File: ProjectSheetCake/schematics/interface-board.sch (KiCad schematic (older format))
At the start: 44 parts, among them P1 CONN_8, P2 CONN_6, P3 CONN_8, P4 CONN_6, P7 X_Y_SERVO, P8 Z_A_SERVO

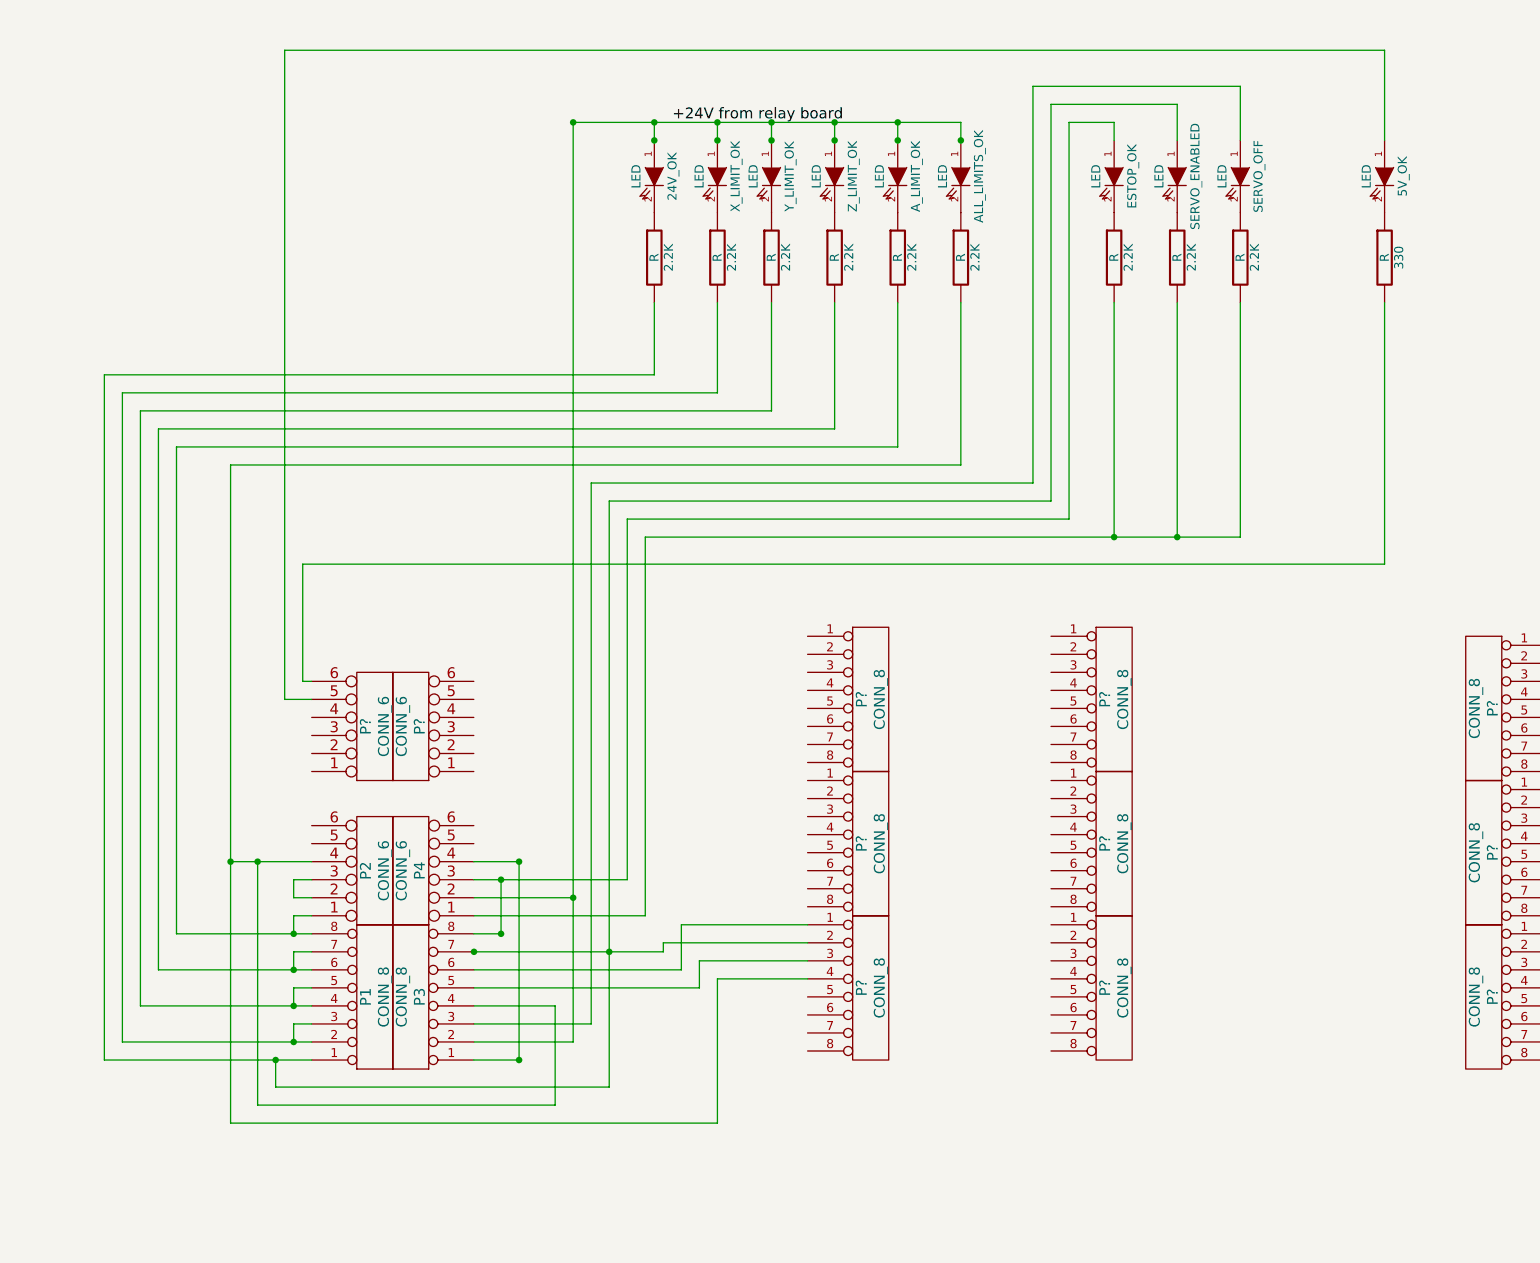
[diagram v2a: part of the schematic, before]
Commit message: Added on-board +5V to the mesa daughter boards
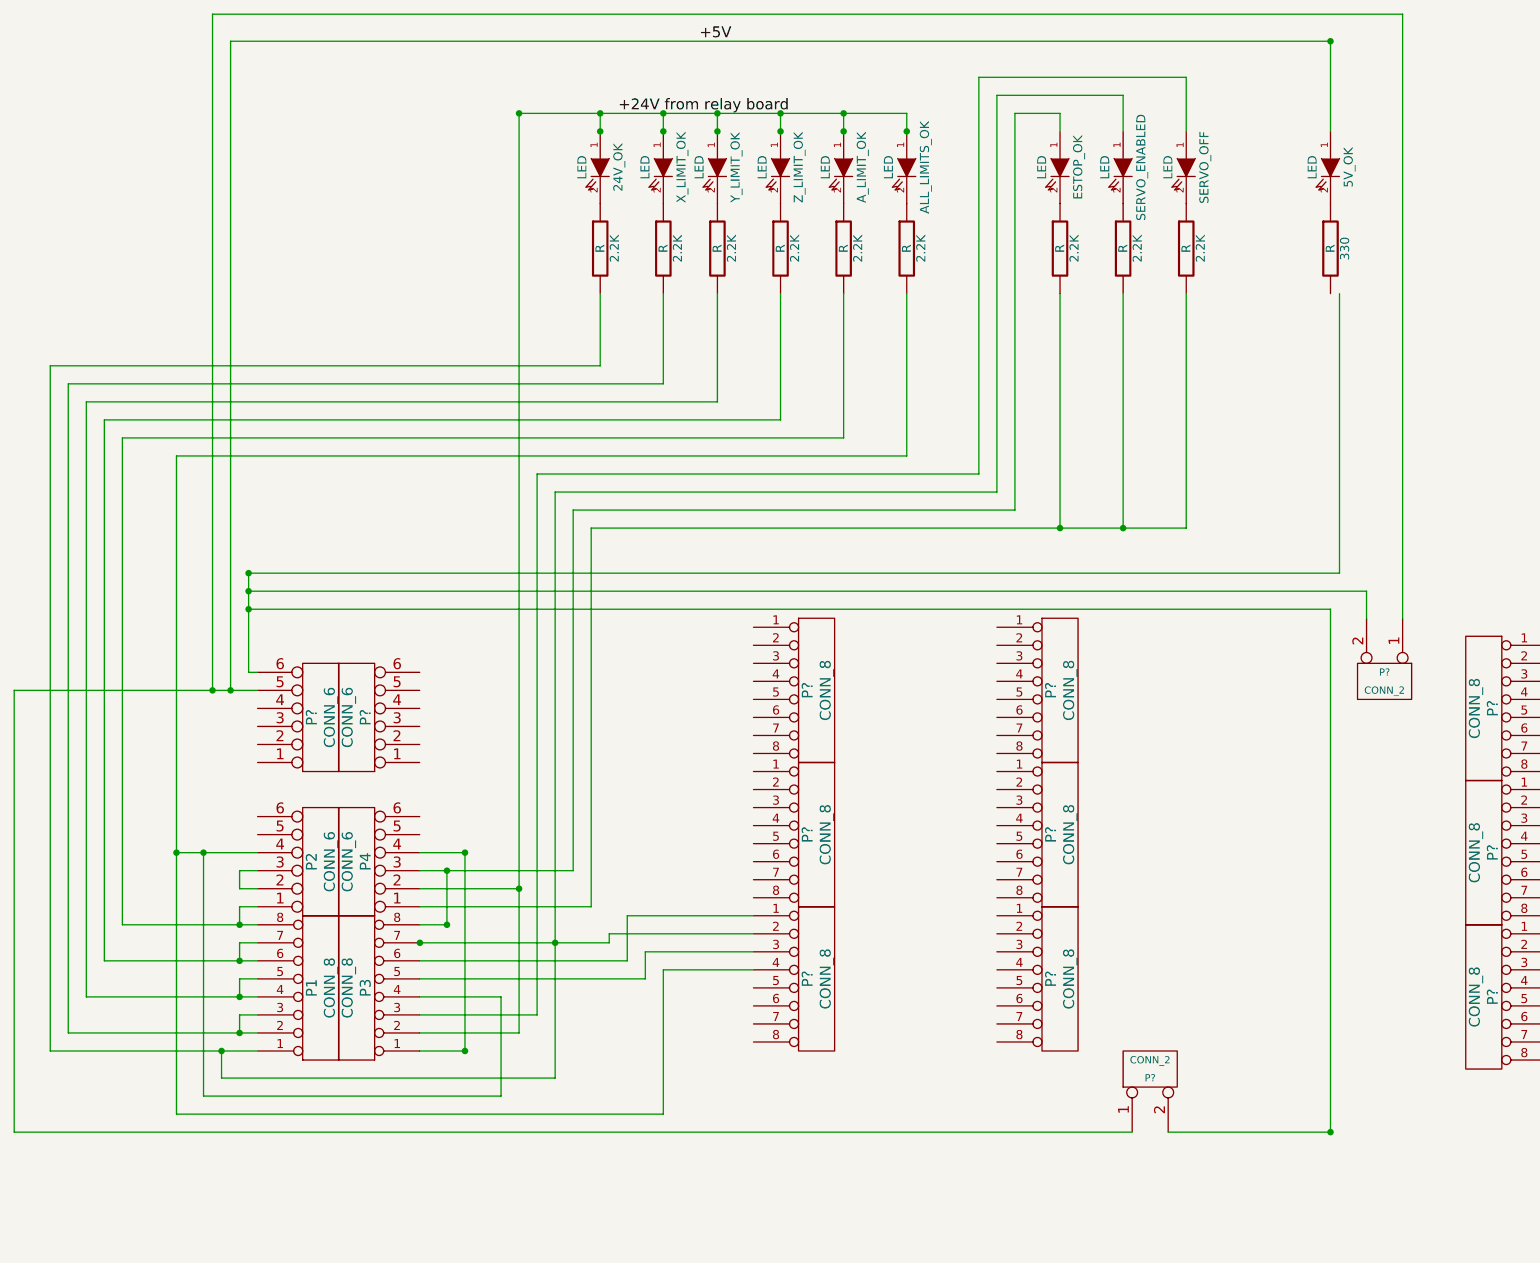
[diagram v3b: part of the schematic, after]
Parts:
- added P? (x2): CONN_2, symbol CONN_2
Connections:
- net labels added: +5V
- wire segments 252 -> 262
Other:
- moved on the sheet: 2.2K, 24V_OK, 330, 5V_OK, ALL_LIMITS_OK, A_LIMIT_OK, ESTOP_OK, P1, P2, P3, P4, P?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

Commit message: fixed an issue with the servo enable indicator LED
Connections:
- wire segments 262 -> 261

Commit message: fix up board layout
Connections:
- wire segments 261 -> 259
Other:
- moved on the sheet: P?
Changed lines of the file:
@@
-EESchema Schematic File Version 2  date 8/15/2011 12:07:04 AM
+EESchema Schematic File Version 2  date 8/15/2011 11:11:12 PM
 LIBS:power
 LIBS:device
@@
 Sheet 1 1
 Title ""
-Date "15 aug 2011"
+Date "16 aug 2011"
 Rev ""
 Comp ""
@@
 $EndDescr
 Wire Notes Line
-	4450 3600 4450 7050
+	11100 7050 8100 7050
 Wire Notes Line
-	7350 3600 4450 3600
+	11100 3600 8100 3600
+Wire Wire Line
+	8500 700  1700 700
+Wire Notes Line
+	4400 3600 7350 3600
+Wire Notes Line
+	4400 3600 4400 7050
+Wire Wire Line
+	4850 5950 4100 5950
+Connection ~ 4000 5750
+Wire Wire Line
+	4000 5750 4850 5750
+Wire Wire Line
+	2850 5850 4850 5850
 Wire Notes Line
 	7350 3600 7350 7050
-Wire Notes Line
-	7800 3600 7800 7050
-Wire Notes Line
-	7800 3600 11100 3600
 Wire Wire Line
 	6750 3350 4000 3350
@@
 	600  6900 6800 6900
 Wire Wire Line
-	8100 4050 8100 3900
+	8300 4050 8300 3900
 Wire Wire Line
 	1900 3800 1900 4350
@@
 Connection ~ 1900 3800
 Wire Wire Line
-	8100 3900 1900 3900
-Wire Wire Line
 	1900 4350 1950 4350
 Wire Wire Line
 	3600 6600 1750 6600
-Wire Wire Line
-	2850 5850 3900 5850
 Connection ~ 2850 5850
 Wire Wire Line
@@
 	11000 1950 12500 1950
 Wire Wire Line
-	12500 1950 12500 1550
-Wire Wire Line
 	10500 5000 10600 5000
 Wire Wire Line
@@
 	3850 1350 3850 1250
 Wire Wire Line
-	4000 5700 4700 5700
-Wire Wire Line
 	2850 5950 4000 5950
 Wire Wire Line
 	1750 6600 1750 6450
 Wire Wire Line
-	4100 5900 4100 6050
-Wire Wire Line
 	1950 5350 1500 5350
 Wire Wire Line
 	1500 6800 4200 6800
 Wire Wire Line
-	4200 6800 4200 6000
-Wire Wire Line
-	4200 6000 4700 6000
-Wire Wire Line
 	2849 6450 3099 6450
 Wire Wire Line
@@
 	3400 1250 5550 1250
 Wire Wire Line
-	4100 5900 4700 5900
-Wire Wire Line
-	4100 6050 2850 6050
+	2850 6050 4100 6050
 Wire Wire Line
 	2850 6150 3300 6150
@@
 	1650 6700 1650 5350
 Connection ~ 1650 5350
-Wire Wire Line
-	3900 5850 3900 5800
-Wire Wire Line
-	3900 5800 4700 5800
 Connection ~ 3000 5750
 Connection ~ 3000 5450
@@
 	7150 4000 7150 6900
 Wire Wire Line
-	8300 4050 8300 700
-Wire Wire Line
-	8300 700  1700 700
+	8500 700  8500 4050
 Wire Wire Line
 	1700 700  1700 4450
@@
 Wire Wire Line
 	4000 5950 4000 3350
-Connection ~ 4000 5700
-Wire Notes Line
-	7350 7050 4450 7050
 Wire Notes Line
 	11100 3600 11100 7050
+Wire Wire Line
+	12500 1950 12500 1500
+Wire Wire Line
+	4850 6050 4200 6050
+Wire Wire Line
+	4200 6050 4200 6800
+Wire Wire Line
+	4100 6050 4100 5950
 Wire Notes Line
-	11100 7050 7800 7050
+	7350 7050 4400 7050
+Wire Wire Line
+	8300 3900 1900 3900
+Wire Notes Line
+	8100 3600 8100 7050
 $Comp
 L CONN_2 P?
@@
 L CONN_2 P?
 U 1 1 4E4601E7
-P 8200 4400
-F 0 "P?" V 8150 4400 40  0000 C CNN
-F 1 "CONN_2" V 8250 4400 40  0000 C CNN
-	1    8200 4400
+P 8400 4400
+F 0 "P?" V 8350 4400 40  0000 C CNN
+F 1 "CONN_2" V 8450 4400 40  0000 C CNN
+	1    8400 4400
 	0    1    1    0
 $EndComp
@@
 L CONN_8 P?
 U 1 1 4E3F5325
-P 6400 6050
-F 0 "P?" V 6350 6050 60  0000 C CNN
-F 1 "CONN_8" V 6450 6050 60  0000 C CNN
-	1    6400 6050
+P 6550 6100
+F 0 "P?" V 6500 6100 60  0000 C CNN
+F 1 "CONN_8" V 6600 6100 60  0000 C CNN
+	1    6550 6100
 	1    0    0    -1
 $EndComp
@@
 L CONN_8 P?
 U 1 1 4E3F5321
-P 6400 5250
-F 0 "P?" V 6350 5250 60  0000 C CNN
-F 1 "CONN_8" V 6450 5250 60  0000 C CNN
-	1    6400 5250
+P 6550 5300
+F 0 "P?" V 6500 5300 60  0000 C CNN
+F 1 "CONN_8" V 6600 5300 60  0000 C CNN
+	1    6550 5300
 	1    0    0    -1
 $EndComp
@@
 L CONN_8 P?
 U 1 1 4E3F531C
-P 6400 4450
-F 0 "P?" V 6350 4450 60  0000 C CNN
-F 1 "CONN_8" V 6450 4450 60  0000 C CNN
-	1    6400 4450
+P 6550 4500
+F 0 "P?" V 6500 4500 60  0000 C CNN
+F 1 "CONN_8" V 6600 4500 60  0000 C CNN
+	1    6550 4500
 	1    0    0    -1
 $EndComp
@@
 L CONN_8 P?
 U 1 1 4E3F5317
-P 5050 6050
-F 0 "P?" V 5000 6050 60  0000 C CNN
-F 1 "CONN_8" V 5100 6050 60  0000 C CNN
-	1    5050 6050
+P 5200 6100
+F 0 "P?" V 5150 6100 60  0000 C CNN
+F 1 "CONN_8" V 5250 6100 60  0000 C CNN
+	1    5200 6100
 	1    0    0    -1
 $EndComp
@@
 L CONN_8 P?
 U 1 1 4E3F5313
-P 5050 5250
-F 0 "P?" V 5000 5250 60  0000 C CNN
-F 1 "CONN_8" V 5100 5250 60  0000 C CNN
-	1    5050 5250
+P 5200 5300
+F 0 "P?" V 5150 5300 60  0000 C CNN
+F 1 "CONN_8" V 5250 5300 60  0000 C CNN
+	1    5200 5300
 	1    0    0    -1
 $EndComp
@@
 L CONN_8 P?
 U 1 1 4E3F530D
-P 5050 4450
-F 0 "P?" V 5000 4450 60  0000 C CNN
-F 1 "CONN_8" V 5100 4450 60  0000 C CNN
-	1    5050 4450
-	1    0    0    -1
-$EndComp
+P 5200 4500
+F 0 "P?" V 5150 4500 60  0000 C CNN
+F 1 "CONN_8" V 5250 4500 60  0000 C CNN
+	1    5200 4500
+	1    0    0    -1
+$EndComp

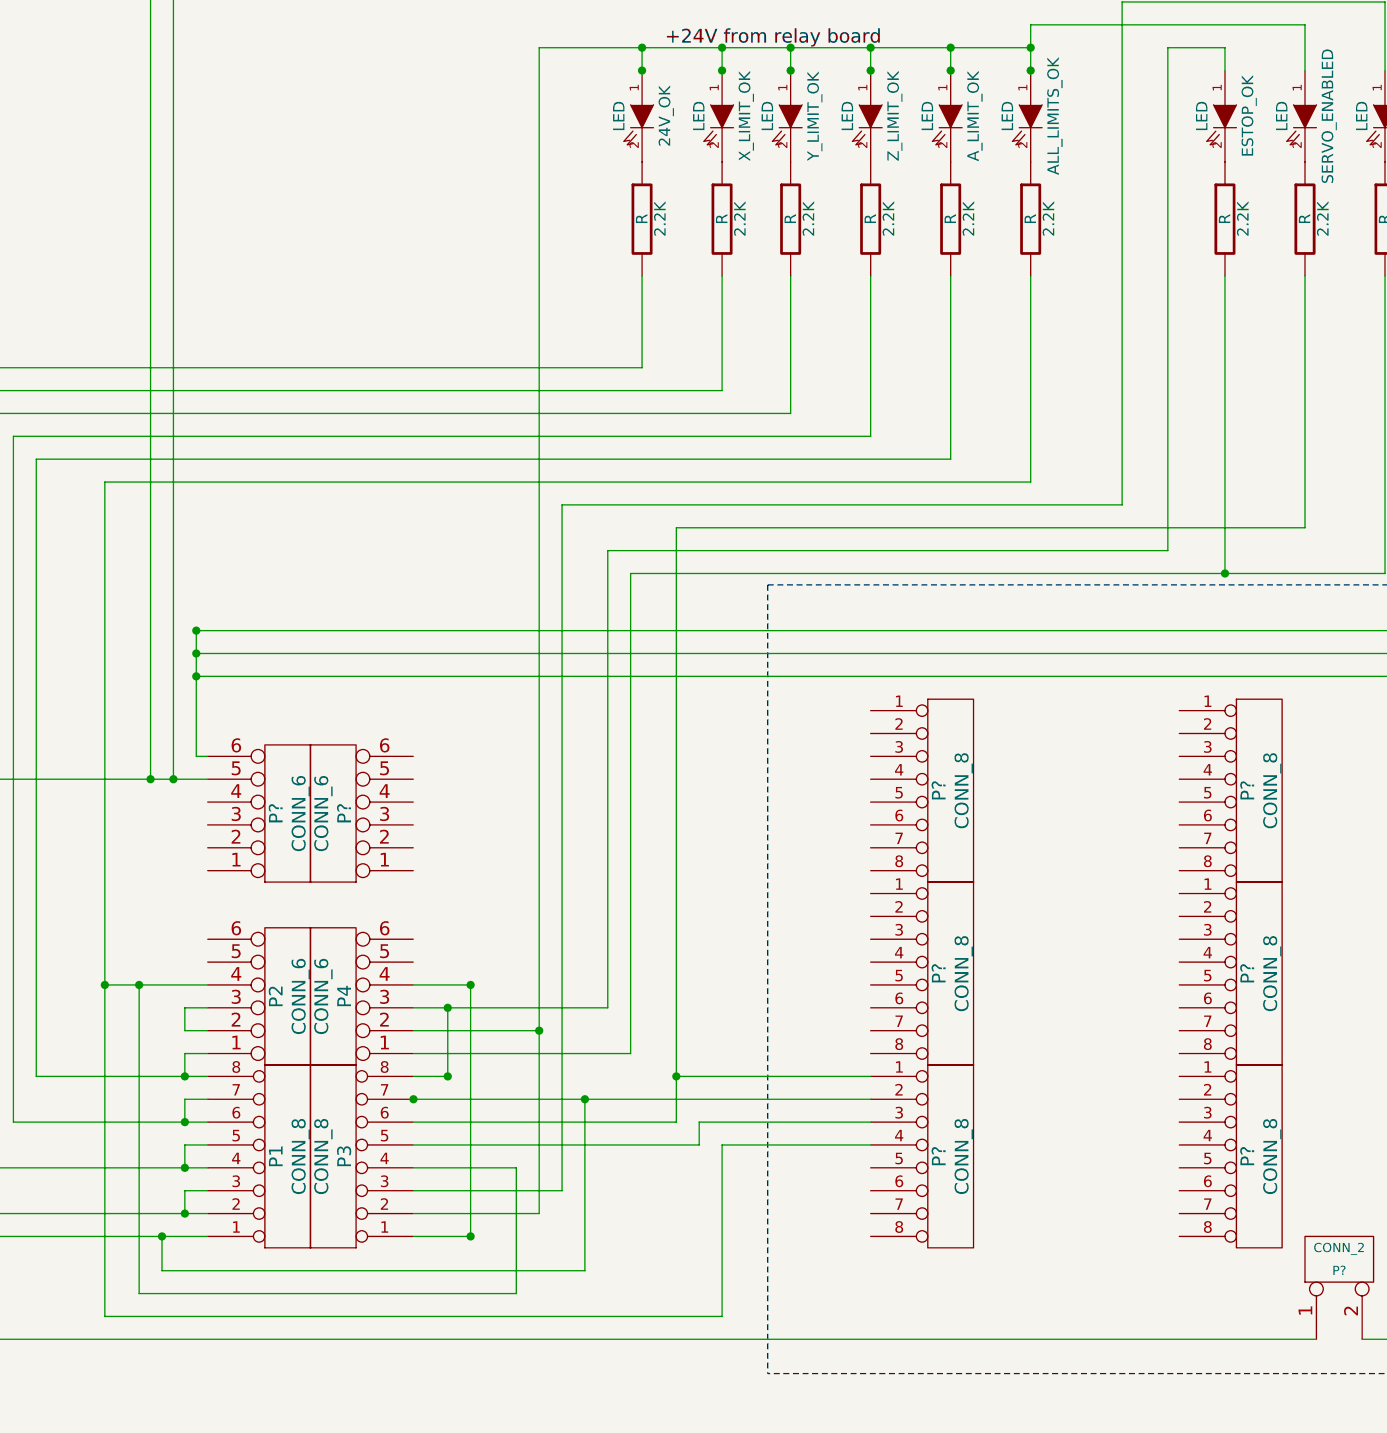
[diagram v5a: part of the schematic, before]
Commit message: added the estop in wiring
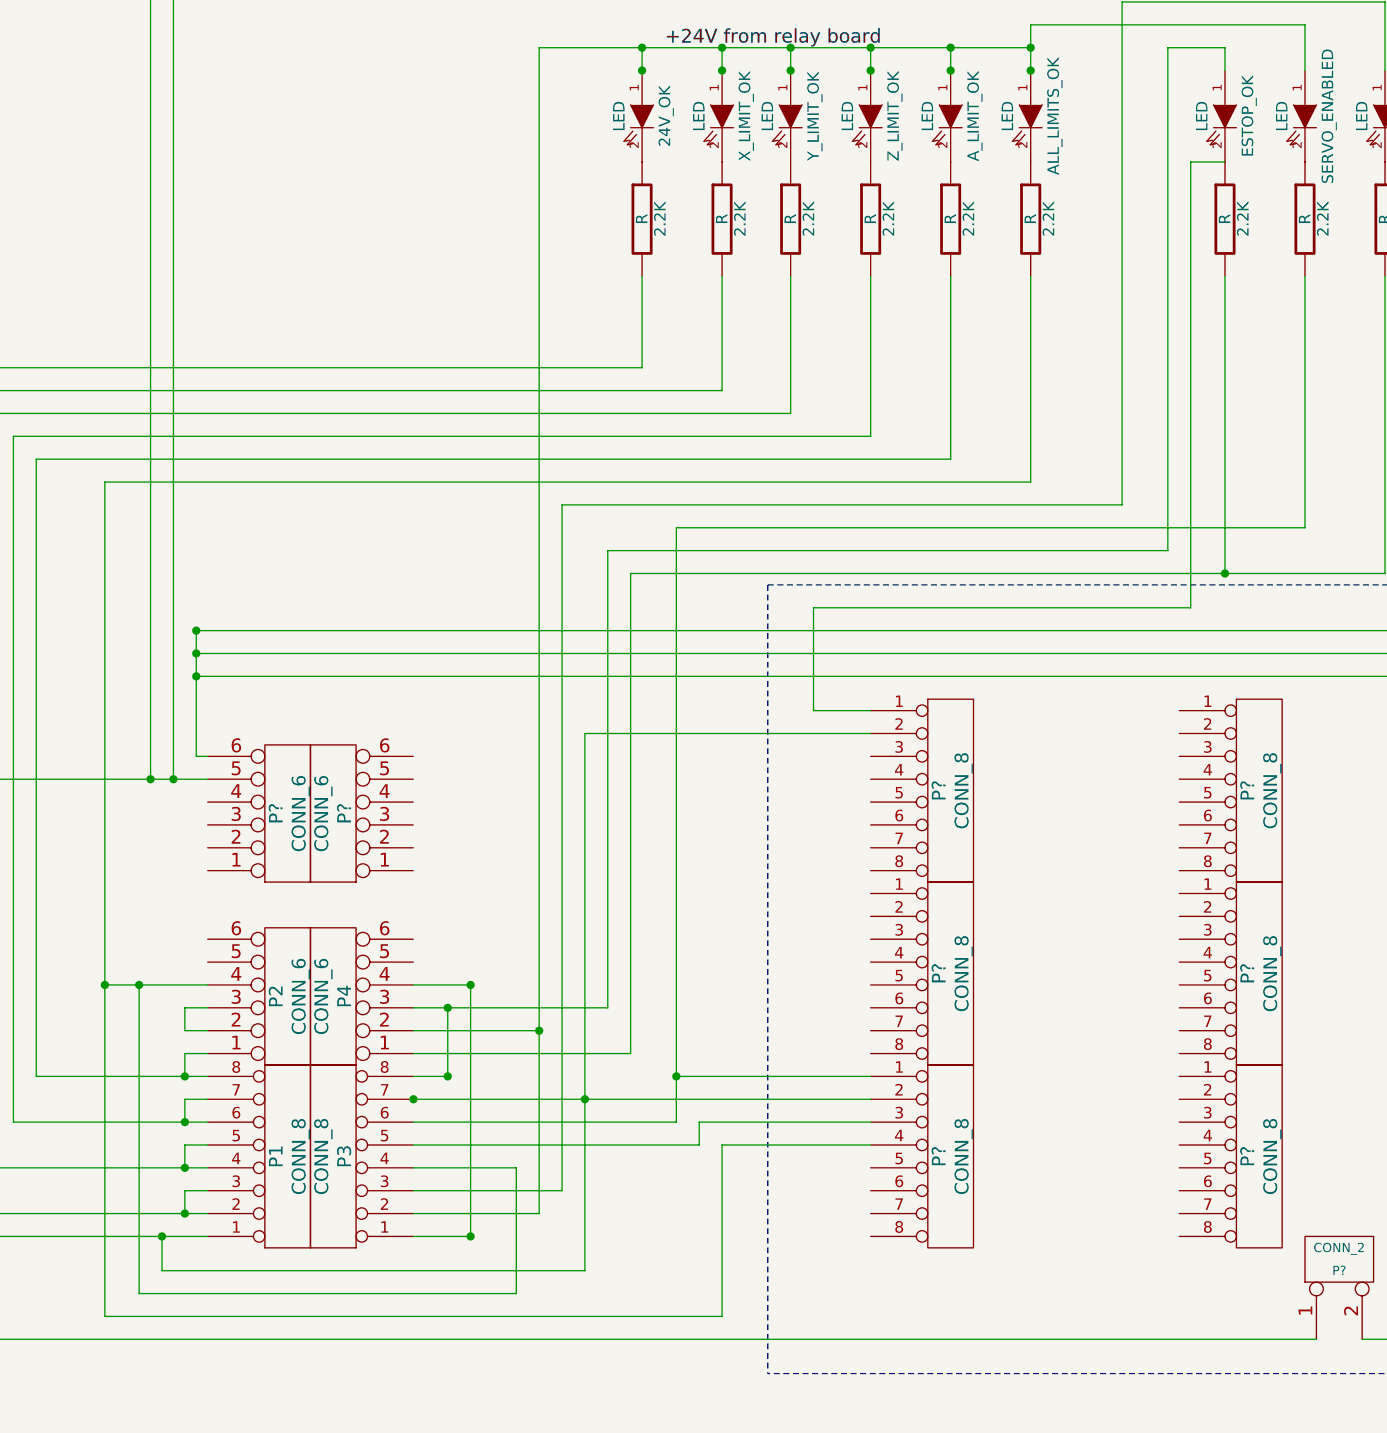
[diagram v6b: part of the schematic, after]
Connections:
- wire segments 259 -> 265
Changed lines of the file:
@@
-EESchema Schematic File Version 2  date 8/15/2011 11:11:12 PM
+EESchema Schematic File Version 2  date 8/16/2011 9:09:40 PM
 LIBS:power
 LIBS:device
@@
 Sheet 1 1
 Title ""
-Date "16 aug 2011"
+Date "17 aug 2011"
 Rev ""
 Comp ""
@@
 Comment4 ""
 $EndDescr
+Wire Wire Line
+	4850 4150 4600 4150
+Wire Wire Line
+	4600 4150 4600 3700
+Wire Wire Line
+	4600 3700 6250 3700
+Wire Wire Line
+	6250 3700 6250 1750
+Wire Wire Line
+	6250 1750 6400 1750
 Wire Notes Line
 	11100 7050 8100 7050
@@
 Connection ~ 3600 5850
 Wire Wire Line
-	3600 5850 3600 6600
-Wire Wire Line
 	6750 3350 6750 2250
 Wire Wire Line
@@
 	1900 4350 1950 4350
 Wire Wire Line
-	3600 6600 1750 6600
+	1750 6600 3600 6600
 Connection ~ 2850 5850
 Wire Wire Line
@@
 Wire Notes Line
 	8100 3600 8100 7050
+Wire Wire Line
+	3600 6600 3600 4250
+Wire Wire Line
+	3600 4250 4850 4250
 $Comp
 L CONN_2 P?
